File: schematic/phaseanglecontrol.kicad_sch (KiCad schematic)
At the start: 43 parts, among them J1 L_supply, J2 N_supply, J3 L_motor, J4 N_motor, K1 shutoff, U1 ATtiny26-16P, Y1 16 MHz

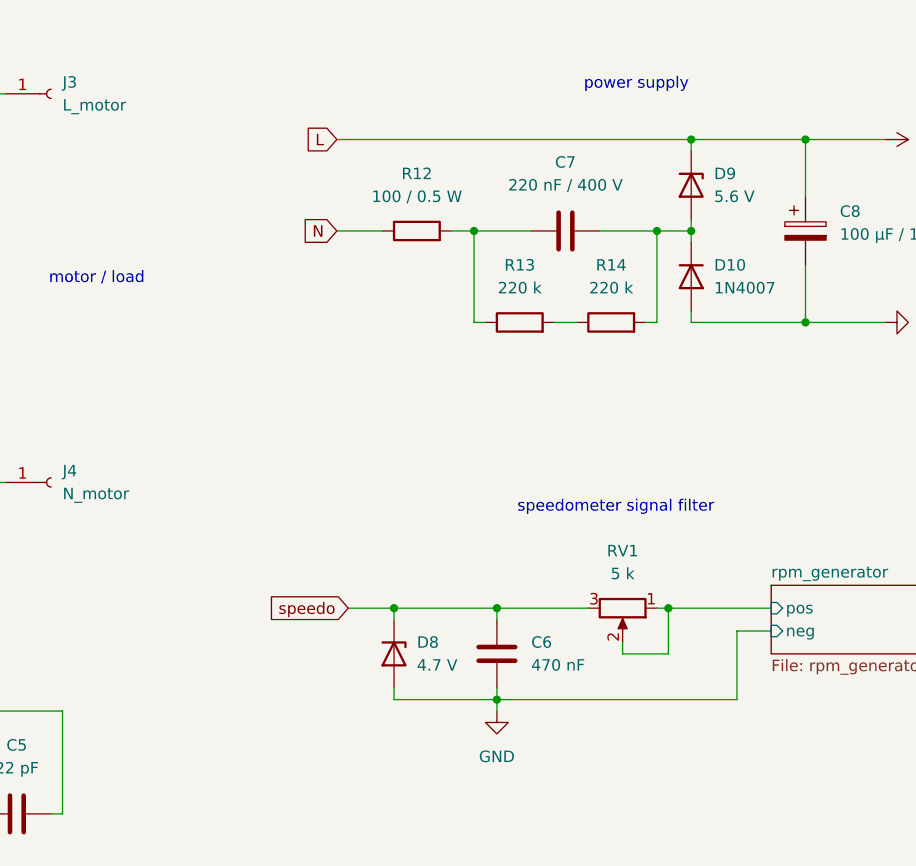
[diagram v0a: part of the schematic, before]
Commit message: schematic: Add schottky to speedo input
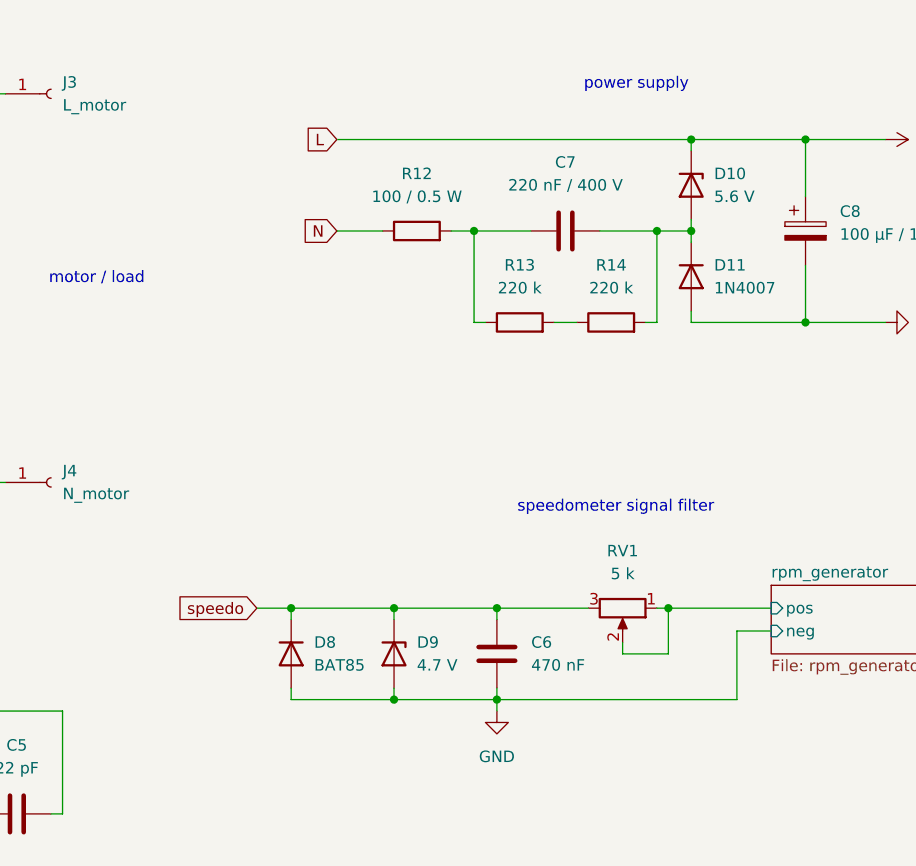
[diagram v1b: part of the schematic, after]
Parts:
- added D8: BAT85, symbol Device:D
- renumbered D9 to D10, D10 to D11, D8 to D9
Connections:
- net GND: now also D8.2 (A)
- net speedo: now also D8.1 (K)
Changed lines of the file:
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@@
 	)
 	(junction
+		(at 210.82 95.25)
+		(diameter 0)
+		(color 0 0 0 0)
+	)
+	(junction
 		(at 116.84 156.21)
 		(diameter 0)
@@
 	)
 	(junction
+		(at 199.39 85.09)
+		(diameter 0)
+		(color 0 0 0 0)
+	)
+	(junction
 		(at 241.3 85.09)
 		(diameter 0)
@@
 	(wire
 		(pts
+			(xy 199.39 95.25) (xy 210.82 95.25)
+		)
+		(stroke
+			(width 0)
+			(type default)
+		)
+	)
+	(wire
+		(pts
 			(xy 222.25 95.25) (xy 222.25 96.52)
 		)
@@
 	(wire
 		(pts
-			(xy 205.74 85.09) (xy 210.82 85.09)
+			(xy 195.58 85.09) (xy 199.39 85.09)
 		)
 		(stroke
@@
 	(wire
 		(pts
+			(xy 199.39 85.09) (xy 210.82 85.09)
+		)
+		(stroke
+			(width 0)
+			(type default)
+		)
+	)
+	(wire
+		(pts
 			(xy 158.75 95.25) (xy 158.75 96.52)
 		)
@@
 	(wire
 		(pts
+			(xy 199.39 93.98) (xy 199.39 95.25)
+		)
+		(stroke
+			(width 0)
+			(type default)
+		)
+	)
+	(wire
+		(pts
 			(xy 158.75 96.52) (xy 173.99 96.52)
 		)
@@
 	(wire
 		(pts
+			(xy 199.39 85.09) (xy 199.39 86.36)
+		)
+		(stroke
+			(width 0)
+			(type default)
+		)
+	)
+	(wire
+		(pts
 			(xy 240.03 43.18) (xy 243.84 43.18)
 		)
@@
 	(global_label "speedo"
 		(shape input)
-		(at 205.74 85.09 180)
+		(at 195.58 85.09 180)
 		(fields_autoplaced yes)
 		(effects
@@
 		)
 		(property "Intersheetrefs" "${INTERSHEET_REFS}"
-			(at 196.1025 85.09 0)
+			(at 185.9425 85.09 0)
 			(effects
 				(font
@@
 	)
 	(symbol
+		(lib_id "Device:D")
+		(at 199.39 90.17 270)
+		(unit 1)
+		(exclude_from_sim no)
+		(in_bom yes)
+		(on_board yes)
+		(dnp no)
+		(fields_autoplaced yes)
+		(property "Reference" "D8"
+			(at 201.93 88.8999 90)
+			(effects
+				(font
+					(size 1.27 1.27)
+				)
+				(justify left)
+			)
+		)
+		(property "Value" "BAT85"
+			(at 201.93 91.4399 90)
+			(effects
+				(font
+					(size 1.27 1.27)
+				)
+				(justify left)
+			)
+		)
+		(property "Footprint" ""
+			(at 199.39 90.17 0)
+			(effects
+				(font
+					(size 1.27 1.27)
+				)
+				(hide yes)
+			)
+		)
+		(property "Datasheet" "~"
+			(at 199.39 90.17 0)
+			(effects
+				(font
+					(size 1.27 1.27)
+				)
+				(hide yes)
+			)
+		)
+		(property "Description" "Diode"
+			(at 199.39 90.17 0)
+			(effects
+				(font
+					(size 1.27 1.27)
+				)
+				(hide yes)
+			)
+		)
+		(property "Sim.Device" "D"
+			(at 199.39 90.17 0)
+			(effects
+				(font
+					(size 1.27 1.27)
+				)
+				(hide yes)
+			)
+		)
+		(property "Sim.Pins" "1=K 2=A"
+			(at 199.39 90.17 0)
+			(effects
+				(font
+					(size 1.27 1.27)
+				)
+				(hide yes)
+			)
+		)
+		(pin "2"
+		)
+		(pin "1"
+		)
+		(instances
+			(project ""
+				(path "/167e0419-9f88-4ea4-ae96-d03af9cd26b8"
+					(reference "D8")
+					(unit 1)
+				)
+			)
+		)
+	)
+	(symbol
 		(lib_id "power:+5V")
 		(at 184.15 128.27 90)
@@
 		(dnp no)
 		(fields_autoplaced yes)
-		(property "Reference" "D9"
+		(property "Reference" "D10"
 			(at 246.38 36.8299 90)
 			(effects
@@
 			(project ""
 				(path "/167e0419-9f88-4ea4-ae96-d03af9cd26b8"
-					(reference "D9")
+					(reference "D10")
 					(unit 1)
 				)
@@
 		(dnp no)
 		(fields_autoplaced yes)
-		(property "Reference" "D8"
+		(property "Reference" "D9"
 			(at 213.36 88.8999 90)
 			(effects
@@
 			(project "phaseanglecontrol"
 				(path "/167e0419-9f88-4ea4-ae96-d03af9cd26b8"
-					(reference "D8")
+					(reference "D9")
 					(unit 1)
 				)
@@
 		(dnp no)
 		(fields_autoplaced yes)
-		(property "Reference" "D10"
+		(property "Reference" "D11"
 			(at 246.38 46.9899 90)
 			(effects
@@
 			(project ""
 				(path "/167e0419-9f88-4ea4-ae96-d03af9cd26b8"
-					(reference "D10")
+					(reference "D11")
 					(unit 1)
 				)

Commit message: Update schematic
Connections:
- net rpm_generator/pos renamed rpm_generator/a
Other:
- sheet rpm_generator ports: added a, b; removed neg, pos
- note added: "TODO: use a differential amplifier?"
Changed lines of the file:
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@@
 (kicad_sch
-	(version 20231120)
+	(version 20250114)
 	(generator "eeschema")
-	(generator_version "8.0")
+	(generator_version "9.0")
 	(paper "A4")
 	(title_block
@@
 		(company "Michael Büsch <m@bues.ch>")
 	)
+	(text "speedometer signal filter"
+		(exclude_from_sim no)
+		(at 235.458 73.914 0)
+		(effects
+			(font
+				(size 1.27 1.27)
+			)
+		)
+	)
+	(text "TODO: shutoff relay"
+		(exclude_from_sim no)
+		(at 82.804 48.768 0)
+		(effects
+			(font
+				(size 1.27 1.27)
+			)
+		)
+	)
+	(text "snubber"
+		(exclude_from_sim no)
+		(at 152.908 49.276 0)
+		(effects
+			(font
+				(size 1.27 1.27)
+			)
+		)
+	)
+	(text "TODO REMOVE R7?"
+		(exclude_from_sim no)
+		(at 95.758 53.34 0)
+		(effects
+			(font
+				(size 1.27 1.27)
+			)
+		)
+	)
+	(text "power supply"
+		(exclude_from_sim no)
+		(at 237.744 26.924 0)
+		(effects
+			(font
+				(size 1.27 1.27)
+			)
+		)
+	)
+	(text "TODO: use a differential amplifier?"
+		(exclude_from_sim no)
+		(at 259.588 100.584 0)
+		(effects
+			(font
+				(size 1.27 1.27)
+			)
+		)
+	)
+	(text "motor / load"
+		(exclude_from_sim no)
+		(at 177.8 48.514 0)
+		(effects
+			(font
+				(size 1.27 1.27)
+			)
+		)
+	)
+	(text "speedometer reference"
+		(exclude_from_sim no)
+		(at 237.49 151.13 0)
+		(effects
+			(font
+				(size 1.27 1.27)
+			)
+		)
+	)
+	(text "RPM setpoint"
+		(exclude_from_sim no)
+		(at 240.792 123.698 0)
+		(effects
+			(font
+				(size 1.27 1.27)
+			)
+		)
+	)
+	(text "mains"
+		(exclude_from_sim no)
+		(at 25.654 49.784 0)
+		(effects
+			(font
+				(size 1.27 1.27)
+			)
+		)
+	)
 	(junction
 		(at 55.88 140.97)
@@
 		)
 	)
-	(text "speedometer signal filter"
-		(exclude_from_sim no)
-		(at 235.458 73.914 0)
-		(effects
-			(font
-				(size 1.27 1.27)
-			)
-		)
-	)
-	(text "TODO: shutoff relay"
-		(exclude_from_sim no)
-		(at 82.804 48.768 0)
-		(effects
-			(font
-				(size 1.27 1.27)
-			)
-		)
-	)
-	(text "snubber"
-		(exclude_from_sim no)
-		(at 152.908 49.276 0)
-		(effects
-			(font
-				(size 1.27 1.27)
-			)
-		)
-	)
-	(text "TODO REMOVE R7?"
-		(exclude_from_sim no)
-		(at 95.758 53.34 0)
-		(effects
-			(font
-				(size 1.27 1.27)
-			)
-		)
-	)
-	(text "power supply"
-		(exclude_from_sim no)
-		(at 237.744 26.924 0)
-		(effects
-			(font
-				(size 1.27 1.27)
-			)
-		)
-	)
-	(text "motor / load"
-		(exclude_from_sim no)
-		(at 177.8 48.514 0)
-		(effects
-			(font
-				(size 1.27 1.27)
-			)
-		)
-	)
-	(text "speedometer reference"
-		(exclude_from_sim no)
-		(at 237.49 151.13 0)
-		(effects
-			(font
-				(size 1.27 1.27)
-			)
-		)
-	)
-	(text "RPM setpoint"
-		(exclude_from_sim no)
-		(at 240.792 123.698 0)
-		(effects
-			(font
-				(size 1.27 1.27)
-			)
-		)
-	)
-	(text "mains"
-		(exclude_from_sim no)
-		(at 25.654 49.784 0)
-		(effects
-			(font
-				(size 1.27 1.27)
-			)
-		)
-	)
 	(global_label "speedo"
 		(shape input)
@@
 		(at 252.73 82.55)
 		(size 19.685 7.62)
+		(exclude_from_sim no)
+		(in_bom yes)
+		(on_board yes)
+		(dnp no)
 		(fields_autoplaced yes)
 		(stroke
@@
 			)
 		)
-		(pin "pos" input
+		(pin "a" input
 			(at 252.73 85.09 180)
 			(effects
@@
 			)
 		)
-		(pin "neg" input
+		(pin "b" input
 			(at 252.73 87.63 180)
 			(effects
@@
 		(at 185.42 116.205)
 		(size 13.335 16.51)
+		(exclude_from_sim no)
+		(in_bom yes)
+		(on_board yes)
+		(dnp no)
 		(fields_autoplaced yes)
 		(stroke
@@
 		)
 	)
+	(embedded_fonts no)
 )

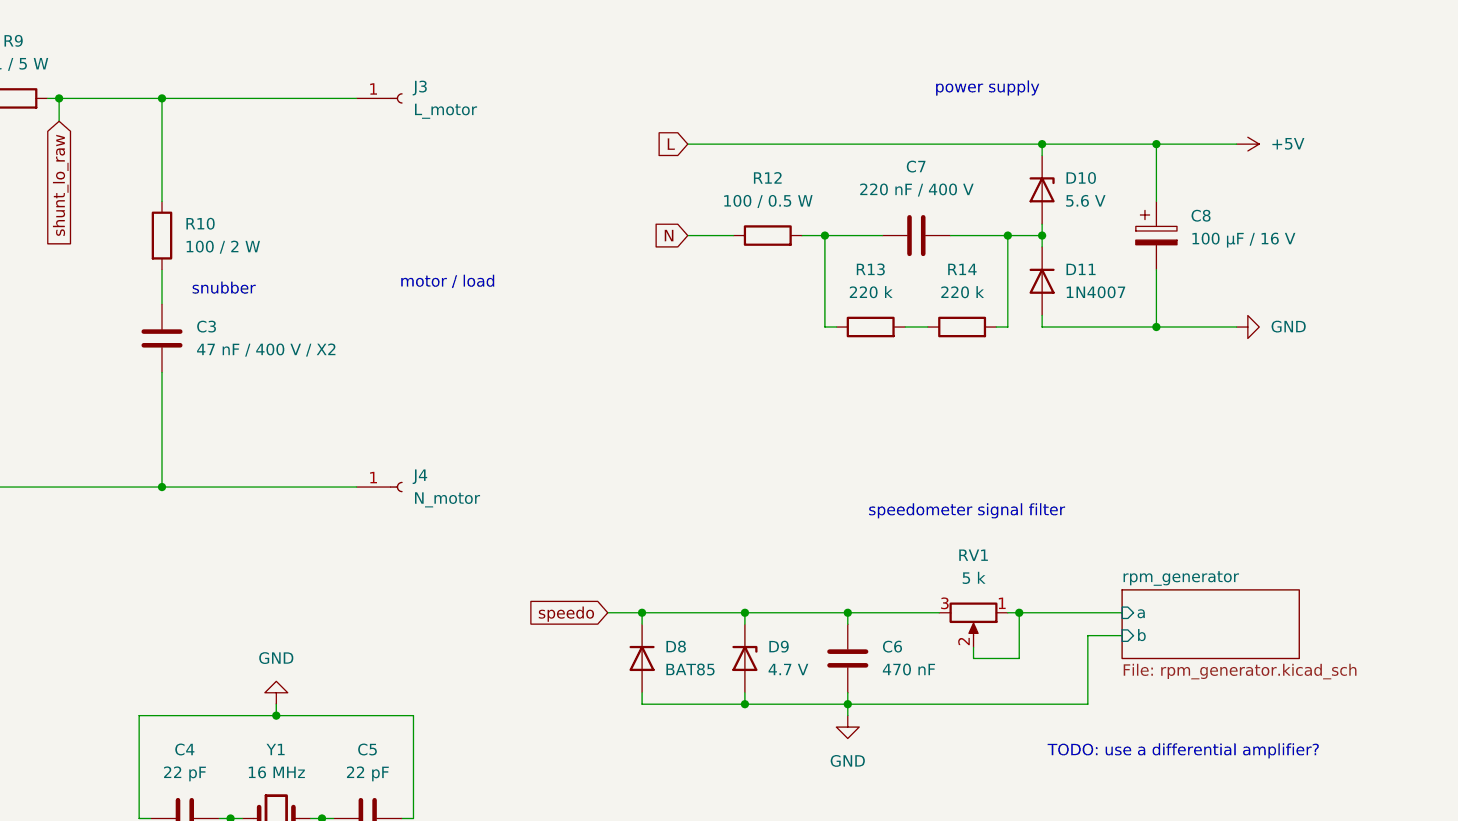
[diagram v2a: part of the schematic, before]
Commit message: Update power supply
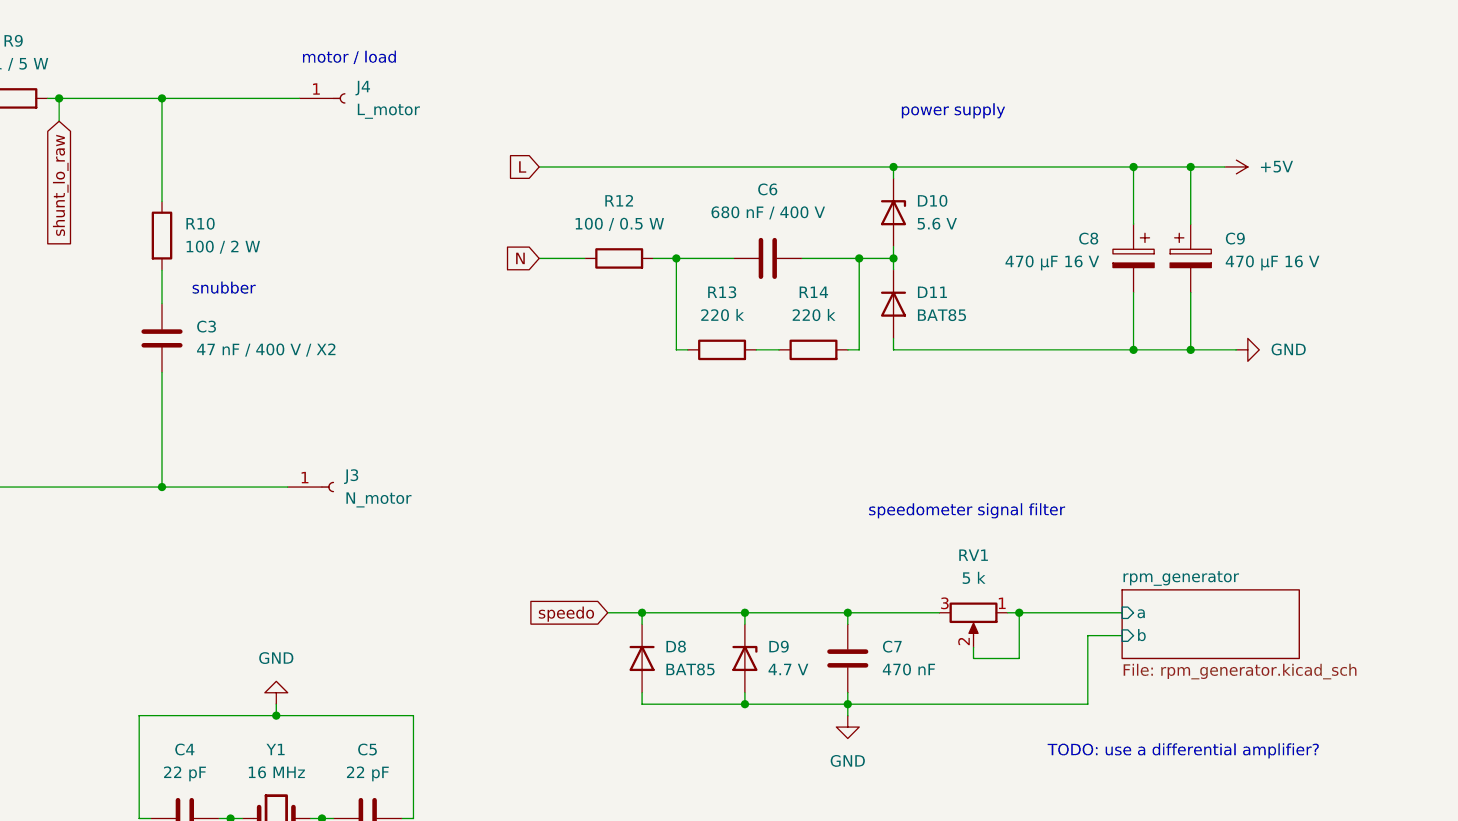
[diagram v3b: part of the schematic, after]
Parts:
- added C8: 470 µF 16 V, symbol Device:C_Polarized
- C6: renamed from C7; value 220 nF / 400 V -> 680 nF / 400 V
- C9: renamed from C8; value 100 µF / 16 V -> 470 µF 16 V
- D11: value 1N4007 -> BAT85
- renumbered C6 to C7, J4 to J3, J3 to J4
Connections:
- net +5V: now also C8.1
- net GND: now also C8.2
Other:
- moved on the sheet: C6, C9, D10, D11, J3, J4, R12, R13, R14

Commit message: Update schematic
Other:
- note added: "WARNING: Pot spindles reaching touchable surfaces must be non-metal and must be capable of insulating 400 V."
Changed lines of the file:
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@@
 	(text "snubber"
 		(exclude_from_sim no)
-		(at 152.908 49.276 0)
+		(at 140.716 57.912 0)
 		(effects
 			(font
@@
 		(effects
 			(font
+				(size 1.27 1.27)
+			)
+		)
+	)
+	(text "WARNING:\nPot spindles reaching touchable surfaces\nmust be non-metal\nand must be capable of insulating 400 V."
+		(exclude_from_sim no)
+		(at 240.284 136.398 0)
+		(effects
+			(font
